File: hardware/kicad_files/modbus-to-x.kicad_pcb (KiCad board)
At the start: 4 copper layers, 55 x 55 mm, 64 parts, among them J1 PWR, J2 UART, J3 Screw_Terminal_3.5mm_2, J4 SSQ-110-X-X-D, SW1 1825910-7, SW2 1825910-7, U1 AMS1117-3.3, U2 ESP32-WROOM-32DM113DH6400PH3Q0, U3 MAX3485, U5 AT24CS64-XHM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

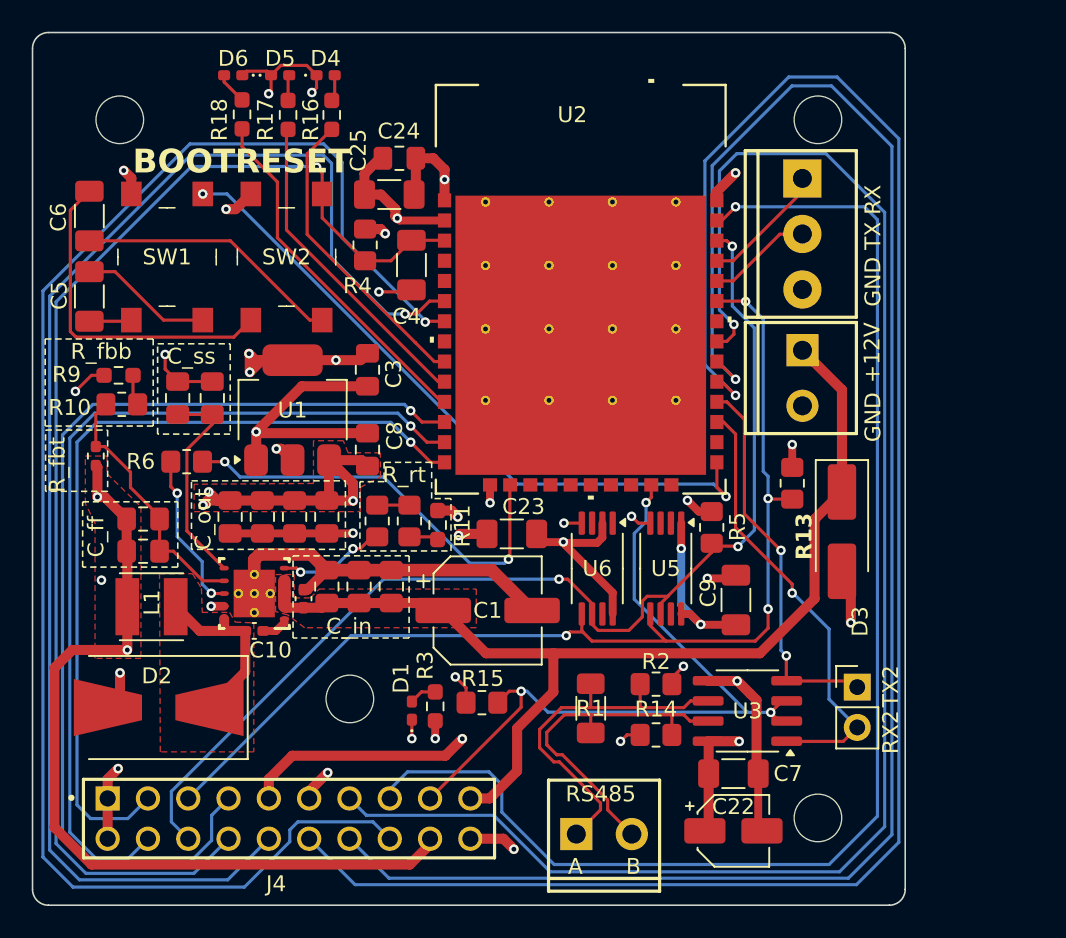
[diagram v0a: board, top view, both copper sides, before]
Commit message: fixed esp32 footprint
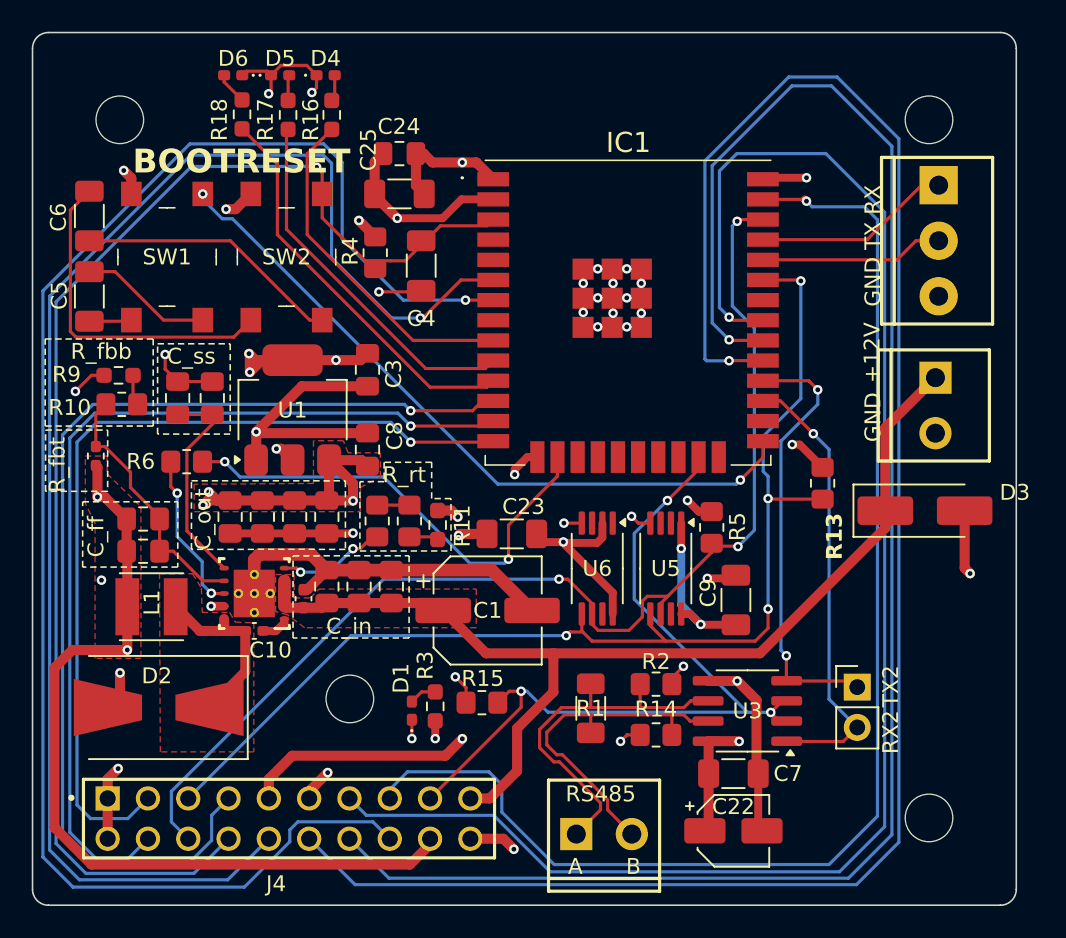
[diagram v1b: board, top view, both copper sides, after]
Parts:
- removed U2: ESP32-WROOM-32DM113DH6400PH3Q0, ESP32-WROOM-32D-M113DH6400PH3Q0:ESP32-WROOM-32DM113DH6400PH3Q0_EXP
- added IC1: ESP32-WROOM-32D_M113DH2800PH3Q0_, footprint_lib:ESP32-WROOM-32D_M113DH2800PH3Q0, F.Cu at (117.5, 97.7)
- C24: value 22uF -> 0.1uF
- C25: value 0.1uF -> 22uF
- moved J2 8.60 mm to (137.1, 89.6)
- moved J1 8.56 mm to (136.9, 101.8)
- moved D3 5.40 mm to (136.2, 110.1), turned to 0 degrees
- moved R13 1.91 mm to (129.8, 108.4)
- moved R4 0.81 mm to (101.6, 93.9)
- moved C25 0.64 mm to (103.1, 90.2)
- moved C4 0.61 mm to (104.5, 94.7)
- moved C24 0.30 mm to (103.1, 87.6)
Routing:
- net /RX_0: track 6.62 -> 11.6 mm
- net /TX_0: track 8.02 -> 12.5 mm
- net /SDA_BUS: track 69.3 -> 73.6 mm
- net VDD33: track 75.1 -> 79.3 mm
- net GND: track 115.4 -> 119.5 mm, vias 26 -> 38
- net /EN: track 79.4 -> 83.4 mm
- net /GPIO_34: track 87.1 -> 90.9 mm
- net /TX_{2}: track 24.0 -> 27.4 mm
- net /PGOOD: track 26.8 -> 30.1 mm
- net /SPI_MOSI: track 84.9 -> 81.8 mm
- net /GPIO27: track 64.6 -> 67.6 mm
- net /RS485_DE_RE: track 47.5 -> 50.5 mm
- net /STAT_2: track 20.3 -> 23.2 mm
- net /GPIO14: track 56.0 -> 58.8 mm
- net /STAT_3: track 22.6 -> 25.3 mm
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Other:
- board size 55 x 55 mm -> 62 x 55 mm

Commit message: small trace improvements using new ESP footprint
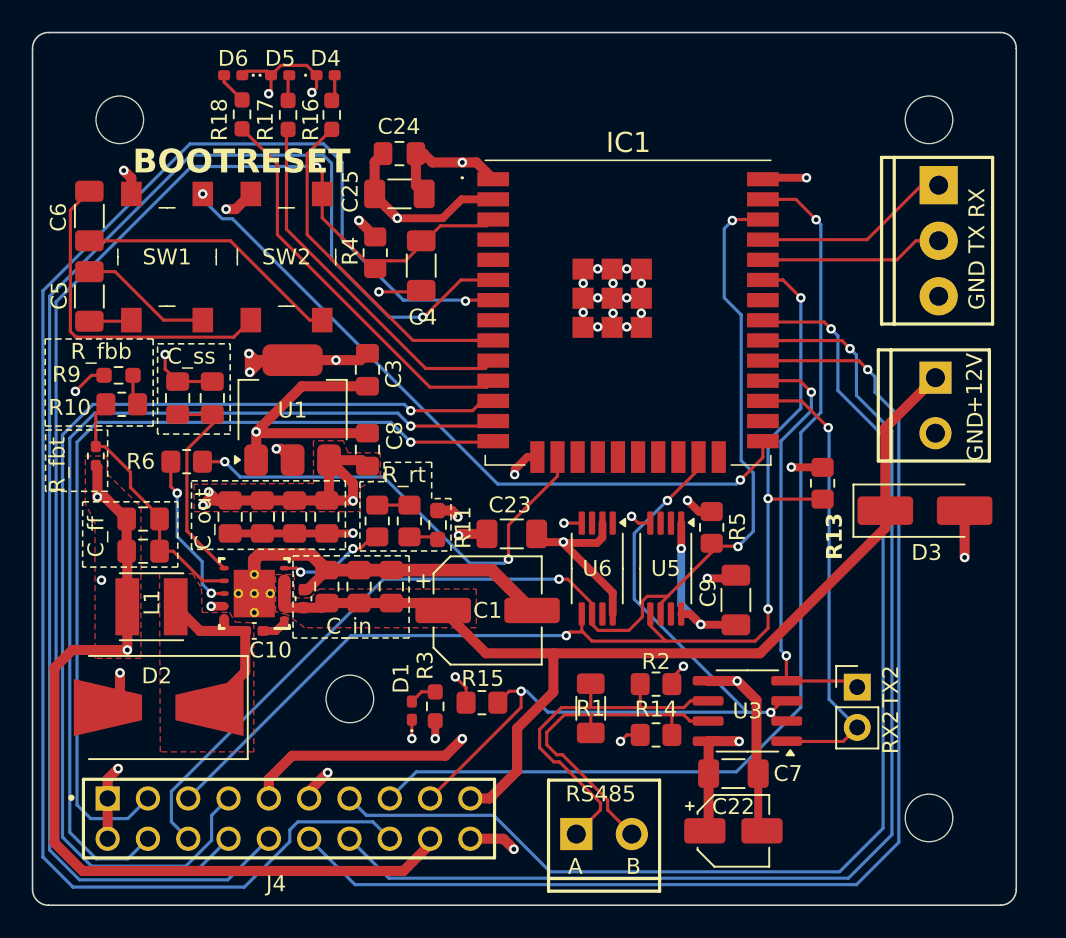
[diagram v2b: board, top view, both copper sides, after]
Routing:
- net /SPI_CS: track 116.0 -> 76.9 mm
- net /SPI_CLK: track 108.3 -> 73.8 mm
- net /SPI_MISO: track 99.6 -> 74.0 mm
- net /SPI_MOSI: track 81.8 -> 63.7 mm
- net GND: track 119.5 -> 118.3 mm
- net VCC5: track 73.5 -> 74.4 mm
- net /SDA_BUS: track 73.6 -> 72.7 mm
- net /RX_{2}: track 28.5 -> 29.3 mm
- net /TX_{2}: track 27.4 -> 26.7 mm
- net /SCL_BUS: track 74.7 -> 75.3 mm
- net VDD33: track 79.3 -> 78.8 mm

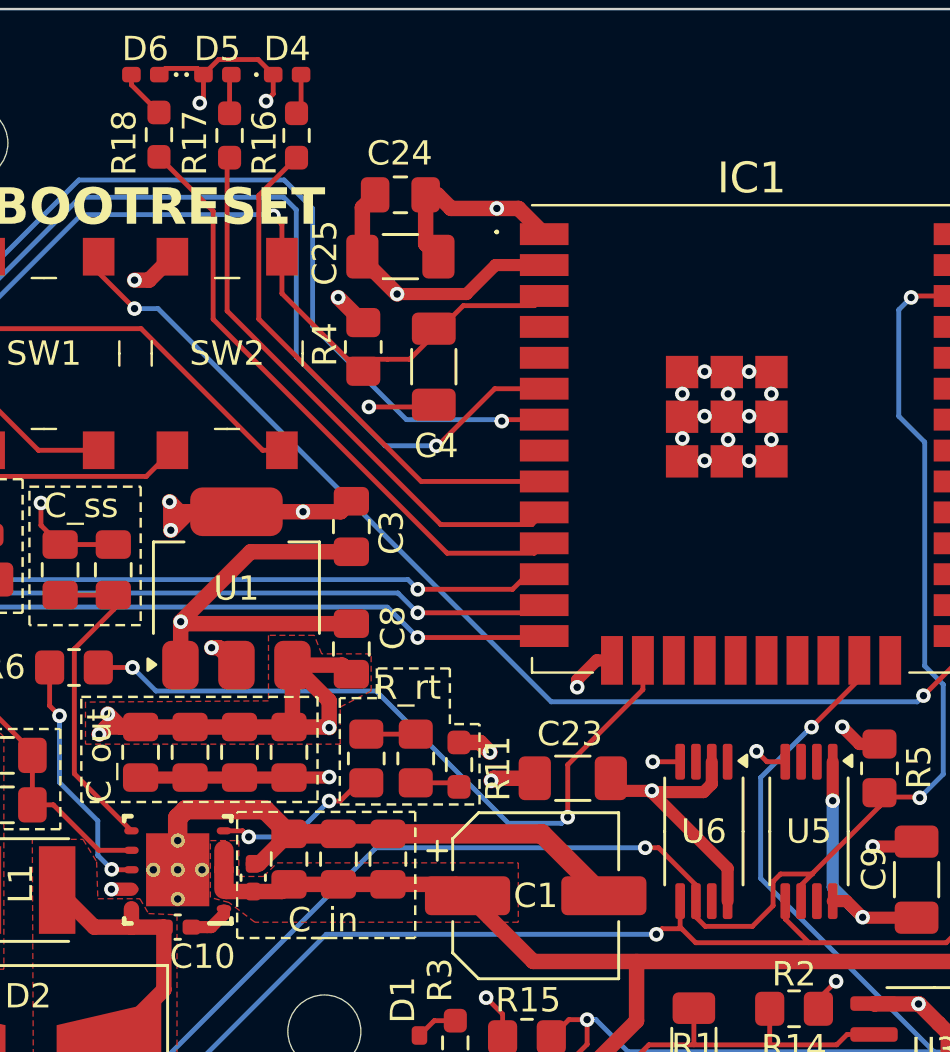
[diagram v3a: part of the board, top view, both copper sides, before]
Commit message: added custom footprints to project to avoid warnings
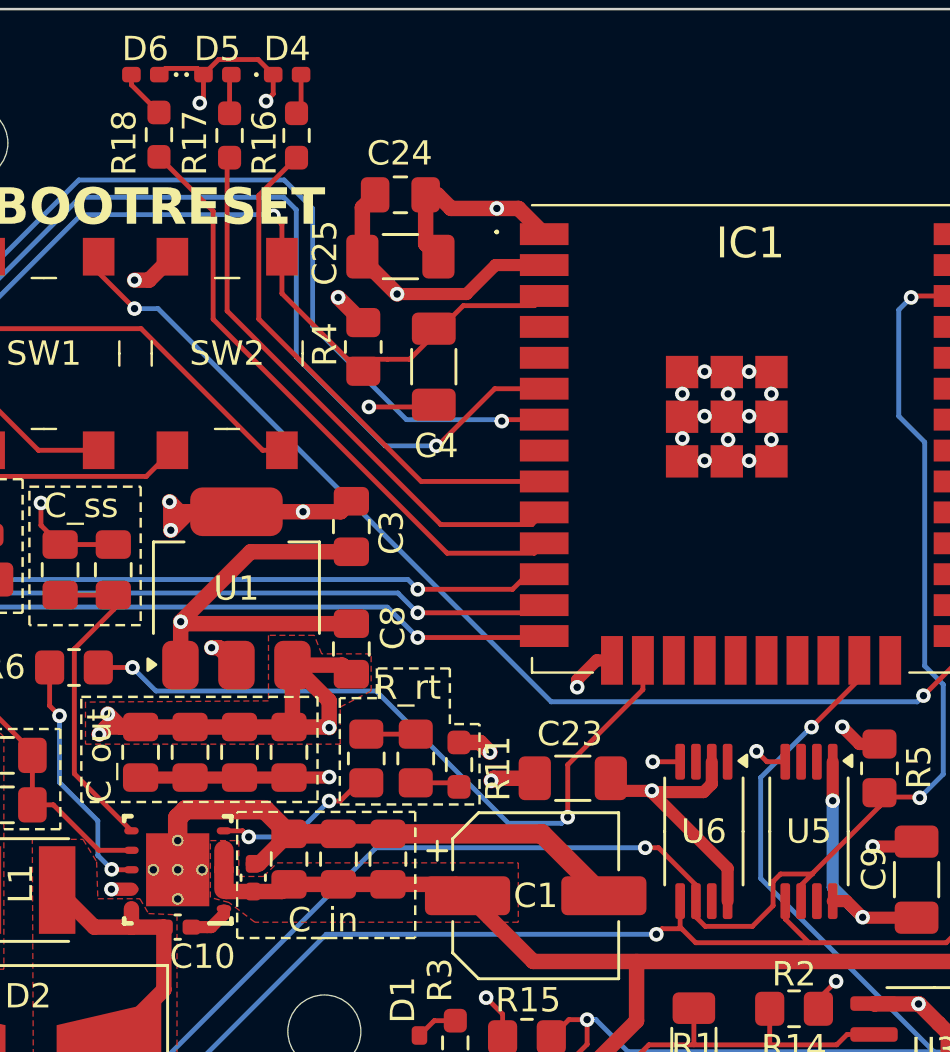
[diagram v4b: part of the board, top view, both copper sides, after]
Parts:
- C19: footprint Capacitor_SMD:C_0402_1005Metric_Pad0.74x0.62mm_HandSolder -> project_footprints:C_0402_1005Metric_Pad0.74x0.62mm_HandSolder
- IC1: footprint footprint_lib:ESP32-WROOM-32D_M113DH2800PH3Q0 -> project_footprints:ESP32-WROOM-32D_M113DH2800PH3Q0
- SW1, SW2: footprint digikey-footprints:Switch_Tactile_SMD_6x6mm_PTS645 -> project_footprints:Switch_Tactile_SMD_6x6mm_PTS645_Modified_Silkscreen
- U7: value LMR14020SQDPRTQ1 -> LMR14020QDPRRQ1; footprint LMR14020SQDPRTQ1:DPR0010A -> project_footprints:LMR14020QDPRRQ1_DPR0010A_Modified_3mm_thermals
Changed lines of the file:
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@@
 		)
 	)
-	(footprint "digikey-footprints:Switch_Tactile_SMD_6x6mm_PTS645"
+	(footprint "project_footprints:Switch_Tactile_SMD_6x6mm_PTS645_Modified_Silkscreen"
 		(layer "F.Cu")
 		(at 96.0077 94.1481 90)
@@
 			)
 		)
-		(property "Footprint" "digikey-footprints:Switch_Tactile_SMD_6x6mm_PTS645"
+		(property "Footprint" "project_footprints:Switch_Tactile_SMD_6x6mm_PTS645_Modified_Silkscreen"
 			(at 0 0 90)
 			(layer "F.Fab")
@@
 		)
 	)
-	(footprint "digikey-footprints:Switch_Tactile_SMD_6x6mm_PTS645"
+	(footprint "project_footprints:Switch_Tactile_SMD_6x6mm_PTS645_Modified_Silkscreen"
 		(layer "F.Cu")
 		(at 88.4787 94.1481 90)
@@
 			)
 		)
-		(property "Footprint" "digikey-footprints:Switch_Tactile_SMD_6x6mm_PTS645"
+		(property "Footprint" "project_footprints:Switch_Tactile_SMD_6x6mm_PTS645_Modified_Silkscreen"
 			(at 0 0 90)
 			(layer "F.Fab")
@@
 		)
 	)
-	(footprint "Capacitor_SMD:C_0402_1005Metric_Pad0.74x0.62mm_HandSolder"
+	(footprint "project_footprints:C_0402_1005Metric_Pad0.74x0.62mm_HandSolder"
 		(layer "F.Cu")
 		(at 97.0788 115.6831 90)
@@
 			)
 		)
-		(property "Footprint" "Capacitor_SMD:C_0402_1005Metric_Pad0.74x0.62mm_HandSolder"
+		(property "Footprint" "project_footprints:C_0402_1005Metric_Pad0.74x0.62mm_HandSolder"
 			(at 0 0 90)
 			(unlocked yes)
@@
 		)
 	)
-	(footprint "LMR14020SQDPRTQ1:DPR0010A"
+	(footprint "project_footprints:LMR14020QDPRRQ1_DPR0010A_Modified_3mm_thermals"
 		(layer "F.Cu")
 		(at 93.9757 115.3571 180)
@@
 			)
 		)
-		(property "Value" "LMR14020SQDPRTQ1"
+		(property "Value" "LMR14020QDPRRQ1"
 			(at 18.161 1.6256 180)
 			(unlocked yes)
@@
 			)
 		)
-		(property "Footprint" "LMR14020SQDPRTQ1:DPR0010A"
+		(property "Footprint" "project_footprints:LMR14020QDPRRQ1_DPR0010A_Modified_3mm_thermals"
 			(at 0 0 0)
 			(layer "F.Fab")
@@
 			)
 		)
-		(property "Datasheet" "LMR14020QDPRRQ1"
+		(property "Datasheet" "https://www.ti.com/lit/gpn/lmr14020-q1"
 			(at 0 0 0)
 			(layer "F.Fab")
@@
 			)
 		)
-		(property "PartNo" "LMR14020Q"
+		(property "PartNo" "LMR14020QDPRRQ1"
 			(at 0 0 180)
 			(unlocked yes)
@@
 		)
 		(fp_text user "U7"
-			(at 0.6561 2.1239 0)
+			(at -0.0043 2.1239 0)
 			(unlocked yes)
 			(layer "F.SilkS")
@@
 			(effects
 				(font
-					(size 1 1)
+					(size 0.8 0.8)
 					(thickness 0.15)
 				)
@@
 		(pad "V" thru_hole circle
 			(at -1.000001 0 180)
-			(size 0.6 0.6)
+			(size 0.499999 0.499999)
 			(drill 0.3)
 			(layers "*.Cu" "*.Mask")
 			(remove_unused_layers no)
 			(net 2 "GND")
-			(pinfunction "GND_STITCH")
-			(pintype "power_in")
 		)
 		(pad "V" thru_hole circle
 			(at 0 -1.2 180)
-			(size 0.6 0.6)
+			(size 0.499999 0.499999)
 			(drill 0.3)
 			(layers "*.Cu" "*.Mask")
 			(remove_unused_layers no)
 			(net 2 "GND")
-			(pinfunction "GND_STITCH")
-			(pintype "power_in")
 		)
 		(pad "V" thru_hole circle
 			(at 0 0 180)
-			(size 0.6 0.6)
+			(size 0.499999 0.499999)
 			(drill 0.3)
 			(layers "*.Cu" "*.Mask")
 			(remove_unused_layers no)
 			(net 2 "GND")
-			(pinfunction "GND_STITCH")
-			(pintype "power_in")
 		)
 		(pad "V" thru_hole circle
 			(at 0 1.2 180)
-			(size 0.6 0.6)
+			(size 0.499999 0.499999)
 			(drill 0.3)
 			(layers "*.Cu" "*.Mask")
 			(remove_unused_layers no)
 			(net 2 "GND")
-			(pinfunction "GND_STITCH")
-			(pintype "power_in")
 		)
 		(pad "V" thru_hole circle
 			(at 0.999998 0 180)
-			(size 0.6 0.6)
+			(size 0.499999 0.499999)
 			(drill 0.3)
 			(layers "*.Cu" "*.Mask")
 			(remove_unused_layers no)
 			(net 2 "GND")
-			(pinfunction "GND_STITCH")
-			(pintype "power_in")
-		)
-		(model "${KIPRJMOD}/lib/3dmodels/LMR14020QDPRRQ1_DPR0010A.stp"
-			(offset
-				(xyz 0 0 0)
-			)
-			(scale
-				(xyz 1 1 1)
-			)
-			(rotate
-				(xyz 0 0 0)
-			)
 		)
 	)
@@
 		)
 	)
-	(footprint "footprint_lib:ESP32-WROOM-32D_M113DH2800PH3Q0"
+	(footprint "project_footprints:ESP32-WROOM-32D_M113DH2800PH3Q0"
 		(layer "F.Cu")
 		(at 117.5318 97.6554)
@@
 		(tags "Integrated Circuit")
 		(property "Reference" "IC1"
-			(at 0.0222 -10.7144 0)
+			(at -0.0314 -8.0442 0)
 			(layer "F.SilkS")
 			(effects
@@
 			)
 		)
-		(property "Footprint" "footprint_lib:ESP32-WROOM-32D_M113DH2800PH3Q0"
+		(property "Footprint" "project_footprints:ESP32-WROOM-32D_M113DH2800PH3Q0"
 			(at 0 0 0)
 			(layer "F.Fab")
@@
 			(pintype "passive")
 		)
-		(model "${KIPRJMOD}/lib/3dmodels/ESP32-WROOM-32D-N16.stp"
+		(model "ESP32-WROOM-32D_M113DH2800PH3Q0_.stp"
 			(offset
-				(xyz 0 3.15 -0.4)
+				(xyz 0 3.150000048 1.6)
 			)
 			(scale

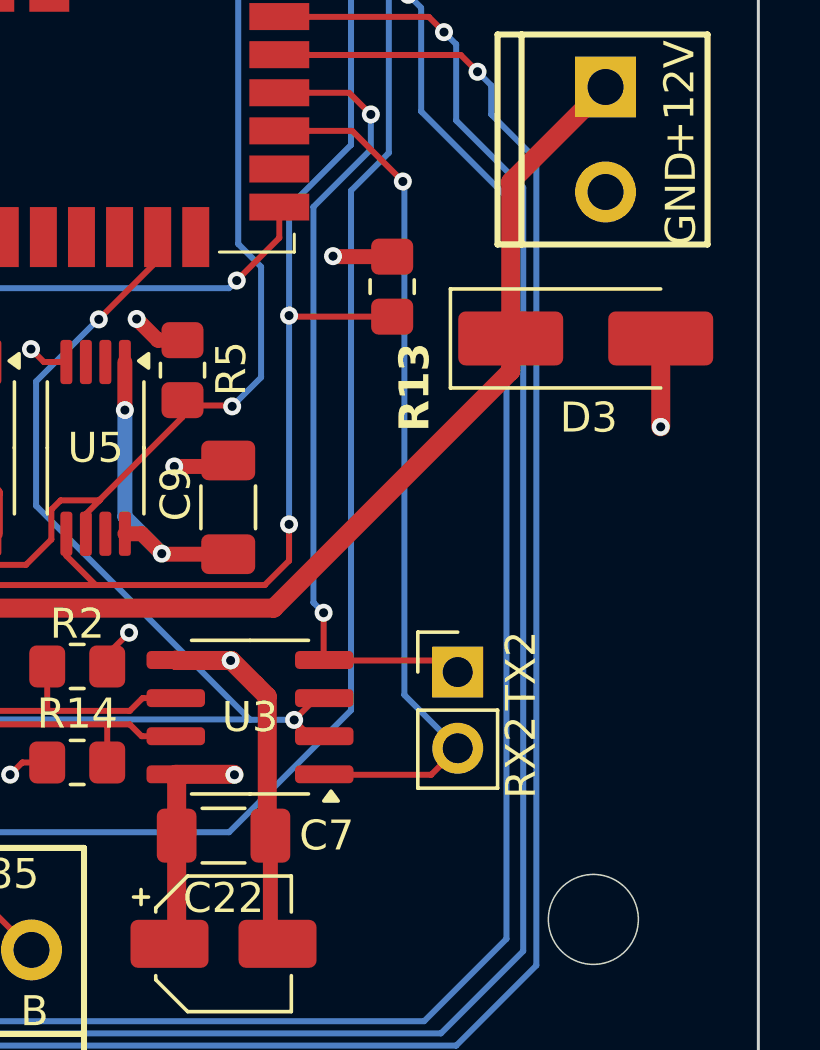
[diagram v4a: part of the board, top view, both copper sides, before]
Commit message: added custom symbols
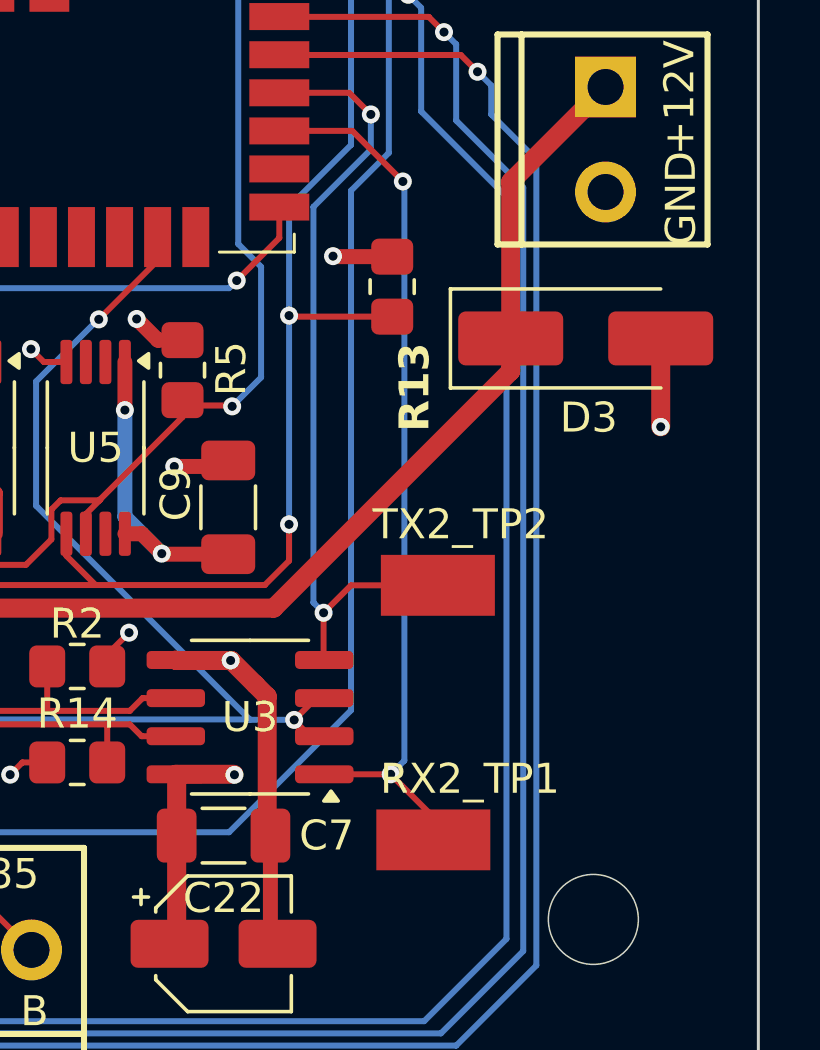
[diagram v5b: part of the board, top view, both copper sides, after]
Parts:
- removed TP_RX2_TX2: TestPoint_2Pole, Connector_PinHeader_2.54mm:PinHeader_1x02_P2.54mm_Vertical
- added RX2_TP1: 5029, project_footprints:KEYSTONE_5029, F.Cu at (131.2, 126.8)
- added TX2_TP2: 5029, project_footprints:KEYSTONE_5029, F.Cu at (131.3, 118.4)
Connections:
- U7 pad V: GND -> (no net)
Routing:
- net /RX_{2}: track 29.3 -> 29.8 mm, vias 1 -> 2
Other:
- board text removed: "RX2"
- board text removed: "TX2"
